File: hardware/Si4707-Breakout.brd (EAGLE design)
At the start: 25.4 x 31.8 mm, 39 parts, among them J3 OUTPUT, J4 ANT, U3 TPA6111, Y1 32.768kHz

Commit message: Production readied
Added fiducials to design. Created production panel.
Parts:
- added JP4, JP5: FIDUCIALUFIDUCIAL, SparkFun:MICRO-FIDUCIAL

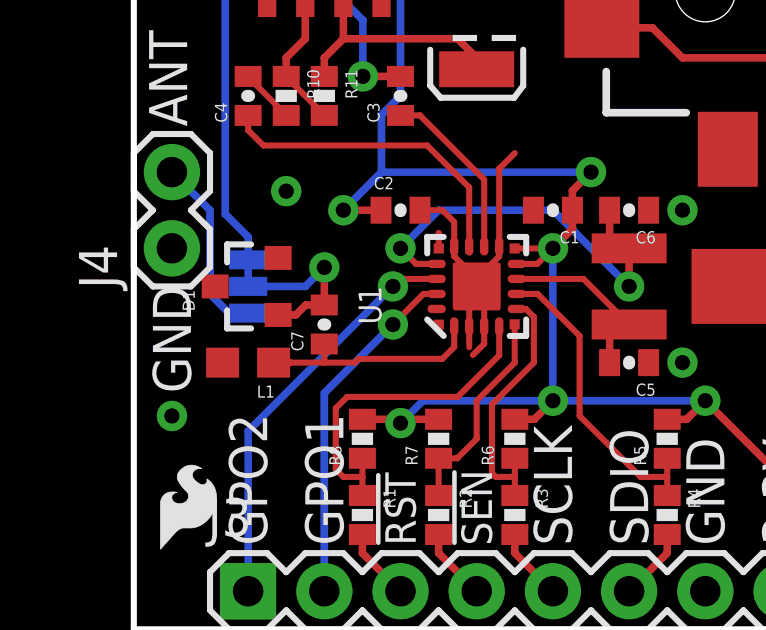
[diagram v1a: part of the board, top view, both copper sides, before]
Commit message: Cleaning up schematic, matching it up to release
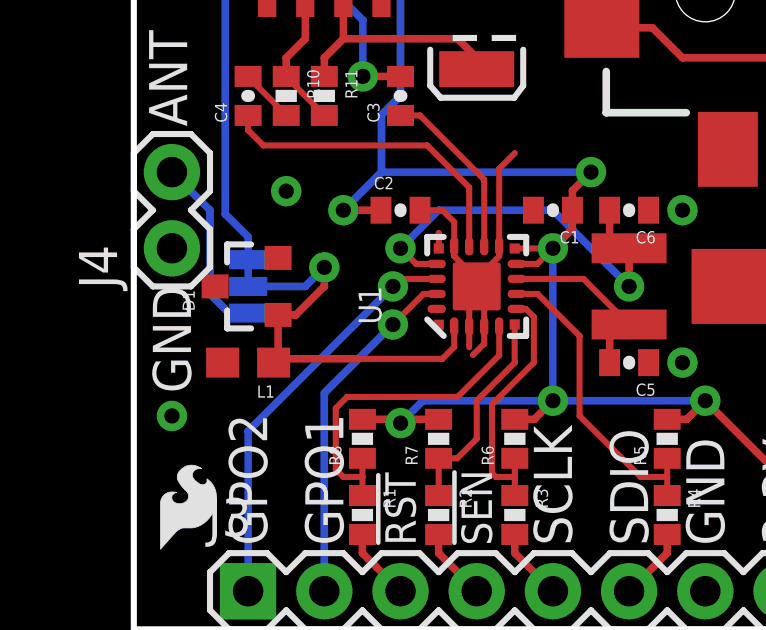
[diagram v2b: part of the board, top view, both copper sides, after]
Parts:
- removed C7: 1nF, SparkFun-Passives:0402-CAP
- removed U$1: CREATIVE_COMMONS, SparkFun-Aesthetics:CREATIVE_COMMONS
- added FRAME1: FRAME-LETTER, SparkFun-Aesthetics:CREATIVE_COMMONS
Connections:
- removed net N$8: C7.1, L1.1, U1.2
- net J1: now also L1.1, U1.2; no longer C7.2
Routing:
- net J1: track 5.73 -> 13.9 mm
- net N$8: track 7.54 -> 0.00 mm
